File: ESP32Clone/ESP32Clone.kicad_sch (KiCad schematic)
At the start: 54 parts, among them J1 Connector, USB-TYPE-C-16P, J2 Conn_01x08_Pin, J3 Conn_01x08_Pin, U1 TPS54331DR, U2 ESP32-C3FH4, U3 AHT20, U4 BH1750FVI-TR, U5 24LC1025-I_SM, X1 40MHz, 15pF

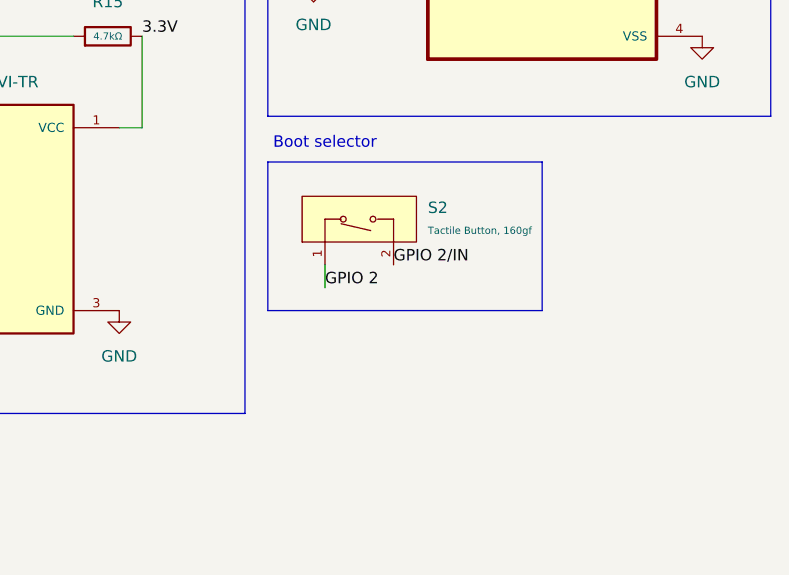
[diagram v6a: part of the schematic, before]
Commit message: added silkscreen
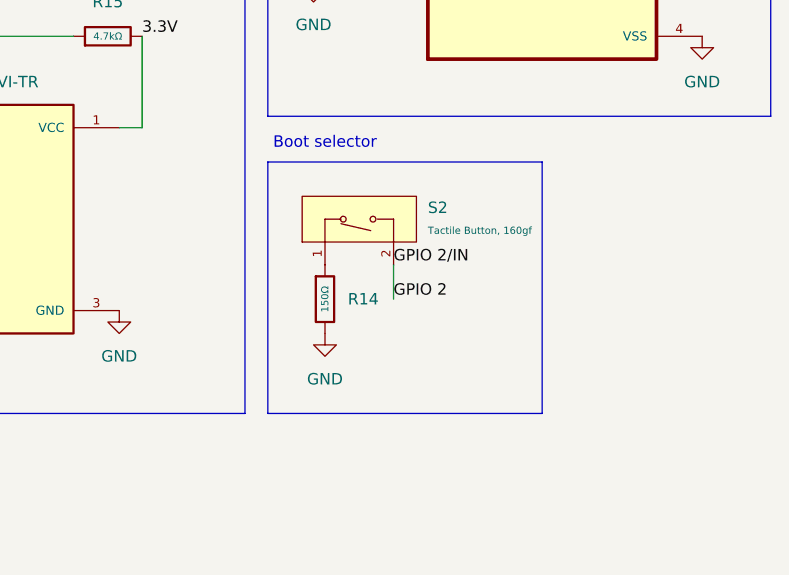
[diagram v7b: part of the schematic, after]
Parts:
- added R14: 150Ω, PCM_JLCPCB:R_0805, symbol PCM_JLCPCB-Resistors:0805,150Ω
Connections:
- net GPIO 2/IN is gone; now on net GPIO 2: S2.2 (B), U2.6 (GPIO2)
- net GND: now also R14.2
- net GPIO 2: no longer S2.1 (A)
- new net: R14.1, S2.1 (A)

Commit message: Added last few 3D files
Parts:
- J2, J3: LCSC (none) -> C18213722
- L1: LCSC (none) -> C2041623
- L2, L5: LCSC (none) -> C1027
- U3: LCSC (none) -> C2757850
- U4: LCSC (none) -> C78960
- U5: LCSC (none) -> C84770
